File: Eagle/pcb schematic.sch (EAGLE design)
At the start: 19 parts

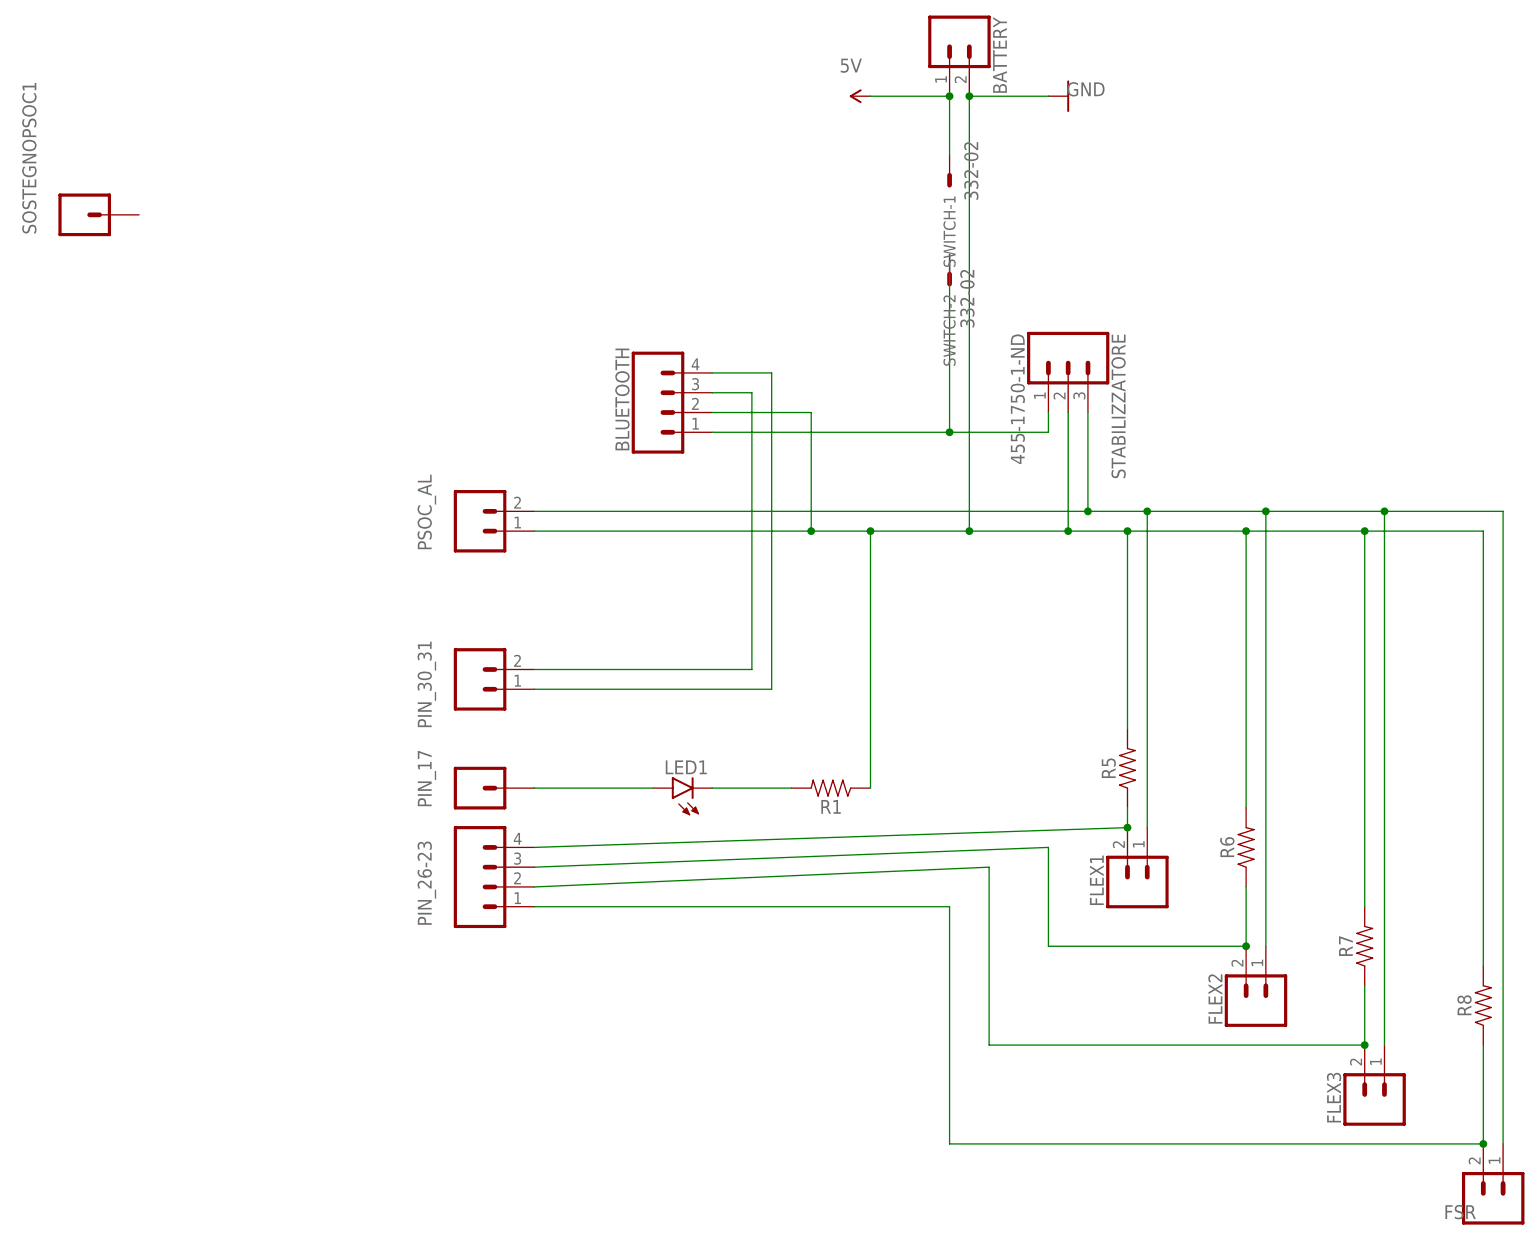
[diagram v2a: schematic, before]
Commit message: PCB con pin separati senza errori
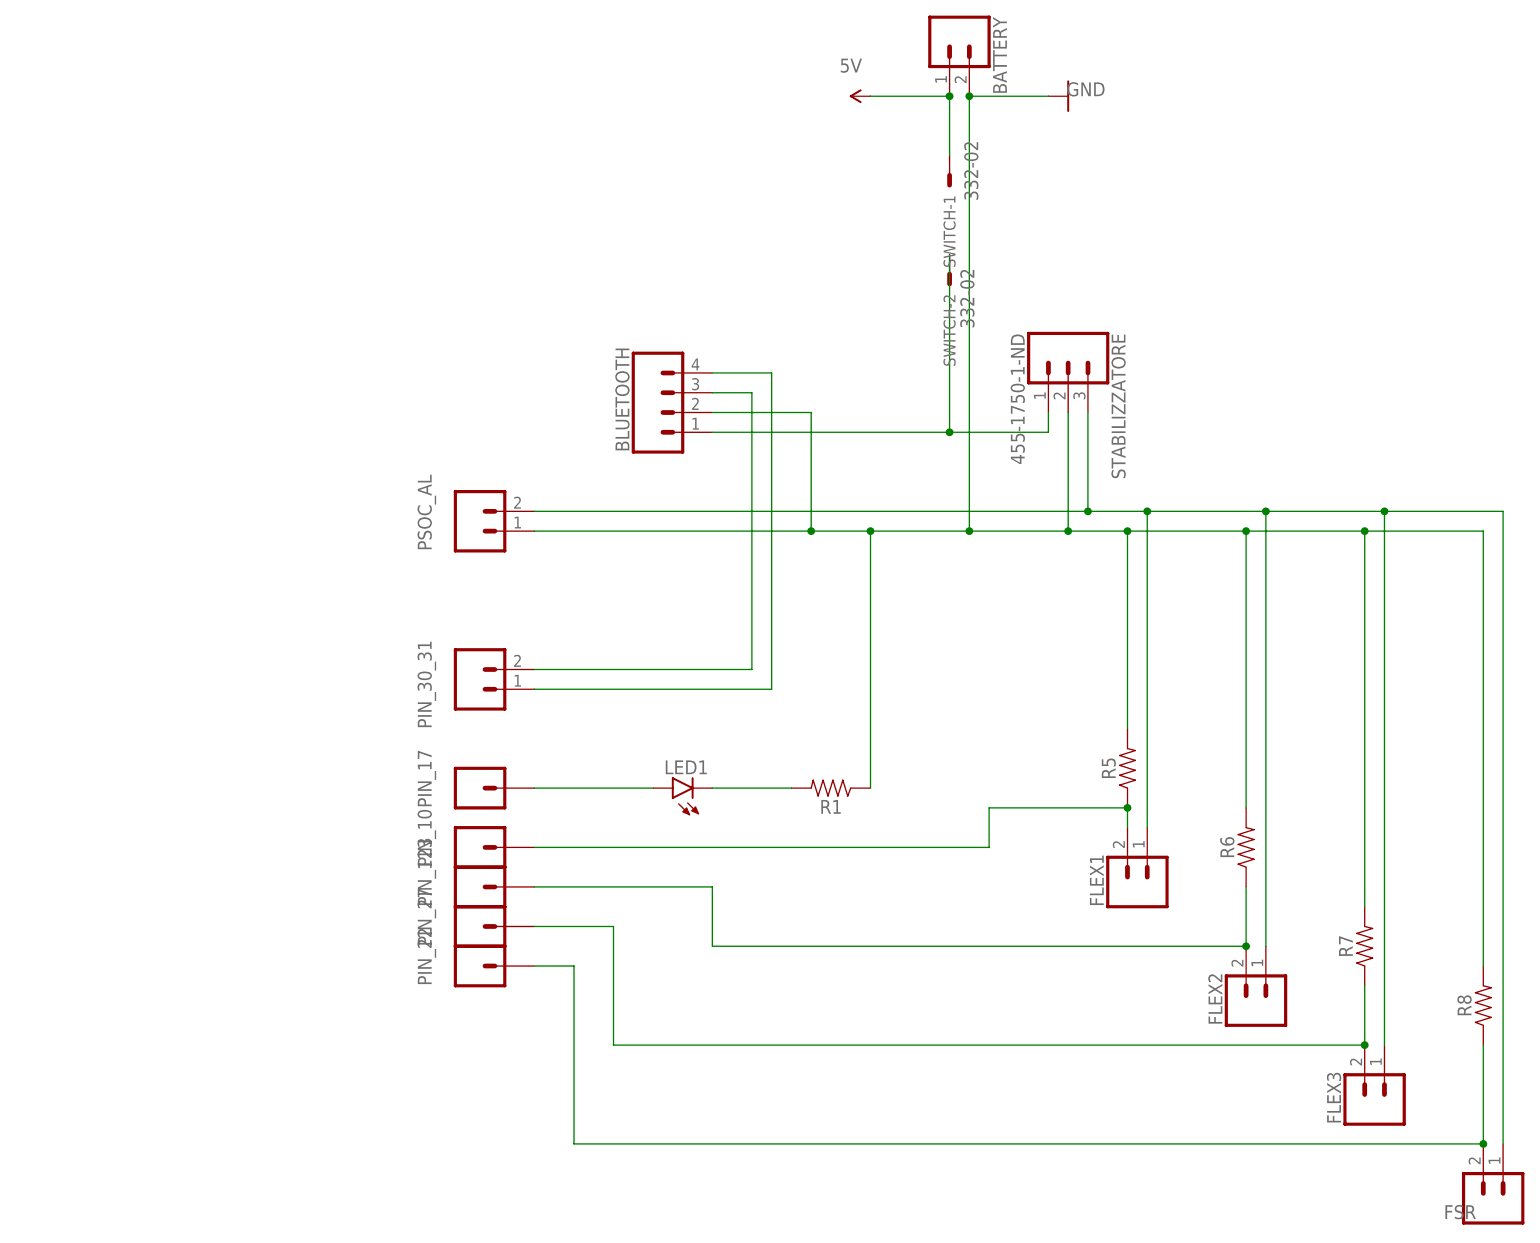
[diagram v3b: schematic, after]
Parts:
- removed PIN_26-23: (no value), SparkFun-Connectors:CONN_04
- removed SOSTEGNOPSOC1: (no value), SparkFun-Connectors:CONN_01
- added PIN_10, PIN_123, PIN_22, PIN_27: (no value), SparkFun-Connectors:CONN_01
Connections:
- net N$1: now also PIN_10.1; no longer PIN_26-23.4
- net N$2: now also PIN_123.1; no longer PIN_26-23.3
- net N$3: now also PIN_27.1; no longer PIN_26-23.2
- net N$5: now also PIN_22.1; no longer PIN_26-23.1
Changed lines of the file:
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@@
 <part name="FSR" library="SparkFun-Connectors" deviceset="CONN_02" device=""/>
 <part name="PSOC_AL" library="SparkFun-Connectors" deviceset="CONN_02" device=""/>
-<part name="PIN_26-23" library="SparkFun-Connectors" deviceset="CONN_04" device=""/>
 <part name="R5" library="SparkFun-Resistors" deviceset="RESISTOR" device="AXIAL-0.3" value=" "/>
 <part name="R6" library="SparkFun-Resistors" deviceset="RESISTOR" device="AXIAL-0.3" value=" "/>
@@
 <part name="LED1" library="led" library_urn="urn:adsk.eagle:library:259" deviceset="LED" device="5MM" package3d_urn="urn:adsk.eagle:package:15799/2"/>
 <part name="SWITCH" library="con-garry" library_urn="urn:adsk.eagle:library:147" deviceset="332-02" device="" package3d_urn="urn:adsk.eagle:package:6810/1"/>
-<part name="SOSTEGNOPSOC1" library="SparkFun-Connectors" deviceset="CONN_01" device=""/>
 <part name="STABILIZZATORE" library="SparkFun-Connectors" deviceset="CONN_03" device="" value="455-1750-1-ND"/>
+<part name="PIN_10" library="SparkFun-Connectors" deviceset="CONN_01" device=""/>
+<part name="PIN_123" library="SparkFun-Connectors" deviceset="CONN_01" device=""/>
+<part name="PIN_27" library="SparkFun-Connectors" deviceset="CONN_01" device=""/>
+<part name="PIN_22" library="SparkFun-Connectors" deviceset="CONN_01" device=""/>
 </parts>
 <sheets>
@@
 <attribute name="NAME" x="-61.468" y="71.12" size="1.778" layer="95" font="vector" rot="R90"/>
 </instance>
-<instance part="PIN_26-23" gate="G$1" x="-53.34" y="27.94" smashed="yes">
-<attribute name="VALUE" x="-58.42" y="20.574" size="1.778" layer="96" font="vector"/>
-<attribute name="NAME" x="-61.468" y="22.86" size="1.778" layer="95" font="vector" rot="R90"/>
-</instance>
 <instance part="R5" gate="G$1" x="27.94" y="43.18" smashed="yes" rot="R90">
 <attribute name="NAME" x="26.416" y="43.18" size="1.778" layer="95" font="vector" rot="R90" align="bottom-center"/>
@@
 <attribute name="VALUE" x="6.477" y="107.442" size="1.778" layer="96" rot="R270"/>
 </instance>
-<instance part="SOSTEGNOPSOC1" gate="G$1" x="-106.68" y="114.3" smashed="yes">
-<attribute name="VALUE" x="-109.22" y="109.474" size="1.778" layer="96" font="vector"/>
-<attribute name="NAME" x="-112.268" y="111.76" size="1.778" layer="95" font="vector" rot="R90"/>
-</instance>
 <instance part="STABILIZZATORE" gate="J$1" x="20.32" y="96.52" smashed="yes" rot="R270">
 <attribute name="VALUE" x="12.954" y="99.06" size="1.778" layer="96" font="vector" rot="R270"/>
 <attribute name="NAME" x="25.908" y="99.06" size="1.778" layer="95" font="vector" rot="R270"/>
+</instance>
+<instance part="PIN_10" gate="G$1" x="-55.88" y="33.02" smashed="yes">
+<attribute name="VALUE" x="-58.42" y="28.194" size="1.778" layer="96" font="vector"/>
+<attribute name="NAME" x="-61.468" y="30.48" size="1.778" layer="95" font="vector" rot="R90"/>
+</instance>
+<instance part="PIN_123" gate="G$1" x="-55.88" y="27.94" smashed="yes">
+<attribute name="VALUE" x="-58.42" y="23.114" size="1.778" layer="96" font="vector"/>
+<attribute name="NAME" x="-61.468" y="25.4" size="1.778" layer="95" font="vector" rot="R90"/>
+</instance>
+<instance part="PIN_27" gate="G$1" x="-55.88" y="22.86" smashed="yes">
+<attribute name="VALUE" x="-58.42" y="18.034" size="1.778" layer="96" font="vector"/>
+<attribute name="NAME" x="-61.468" y="20.32" size="1.778" layer="95" font="vector" rot="R90"/>
+</instance>
+<instance part="PIN_22" gate="G$1" x="-55.88" y="17.78" smashed="yes">
+<attribute name="VALUE" x="-58.42" y="12.954" size="1.778" layer="96" font="vector"/>
+<attribute name="NAME" x="-61.468" y="15.24" size="1.778" layer="95" font="vector" rot="R90"/>
 </instance>
 </instances>
@@
 <net name="N$2" class="0">
 <segment>
-<pinref part="PIN_26-23" gate="G$1" pin="3"/>
-<wire x1="-48.26" y1="30.48" x2="17.78" y2="33.02" width="0.1524" layer="91"/>
-<wire x1="17.78" y1="33.02" x2="17.78" y2="20.32" width="0.1524" layer="91"/>
 <pinref part="FLEX2" gate="G$1" pin="2"/>
-<wire x1="17.78" y1="20.32" x2="43.18" y2="20.32" width="0.1524" layer="91"/>
 <pinref part="R6" gate="G$1" pin="1"/>
 <wire x1="43.18" y1="20.32" x2="43.18" y2="27.94" width="0.1524" layer="91"/>
 <junction x="43.18" y="20.32"/>
+<wire x1="43.18" y1="20.32" x2="-25.4" y2="20.32" width="0.1524" layer="91"/>
+<wire x1="-25.4" y1="20.32" x2="-25.4" y2="27.94" width="0.1524" layer="91"/>
+<pinref part="PIN_123" gate="G$1" pin="1"/>
+<wire x1="-25.4" y1="27.94" x2="-48.26" y2="27.94" width="0.1524" layer="91"/>
 </segment>
 </net>
 <net name="N$3" class="0">
 <segment>
-<pinref part="PIN_26-23" gate="G$1" pin="2"/>
-<wire x1="-48.26" y1="27.94" x2="10.16" y2="30.48" width="0.1524" layer="91"/>
 <pinref part="FLEX3" gate="G$1" pin="2"/>
-<wire x1="10.16" y1="30.48" x2="10.16" y2="7.62" width="0.1524" layer="91"/>
-<wire x1="10.16" y1="7.62" x2="58.42" y2="7.62" width="0.1524" layer="91"/>
 <pinref part="R7" gate="G$1" pin="1"/>
 <wire x1="58.42" y1="15.24" x2="58.42" y2="7.62" width="0.1524" layer="91"/>
 <junction x="58.42" y="7.62"/>
+<wire x1="58.42" y1="7.62" x2="-38.1" y2="7.62" width="0.1524" layer="91"/>
+<wire x1="-38.1" y1="7.62" x2="-38.1" y2="22.86" width="0.1524" layer="91"/>
+<pinref part="PIN_27" gate="G$1" pin="1"/>
+<wire x1="-38.1" y1="22.86" x2="-48.26" y2="22.86" width="0.1524" layer="91"/>
 </segment>
 </net>
 <net name="N$1" class="0">
 <segment>
-<pinref part="PIN_26-23" gate="G$1" pin="4"/>
 <pinref part="FLEX1" gate="G$1" pin="2"/>
-<wire x1="-48.26" y1="33.02" x2="27.94" y2="35.56" width="0.1524" layer="91"/>
 <pinref part="R5" gate="G$1" pin="1"/>
-<junction x="27.94" y="35.56"/>
 <wire x1="27.94" y1="38.1" x2="27.94" y2="35.56" width="0.1524" layer="91"/>
+<pinref part="PIN_10" gate="G$1" pin="1"/>
+<wire x1="-48.26" y1="33.02" x2="10.16" y2="33.02" width="0.1524" layer="91"/>
+<wire x1="10.16" y1="33.02" x2="10.16" y2="38.1" width="0.1524" layer="91"/>
+<wire x1="10.16" y1="38.1" x2="27.94" y2="38.1" width="0.1524" layer="91"/>
+<junction x="27.94" y="38.1"/>
 </segment>
 </net>
@@
 <net name="N$5" class="0">
 <segment>
-<pinref part="PIN_26-23" gate="G$1" pin="1"/>
-<wire x1="-48.26" y1="25.4" x2="5.08" y2="25.4" width="0.1524" layer="91"/>
 <pinref part="FSR" gate="G$1" pin="2"/>
-<wire x1="73.66" y1="-5.08" x2="5.08" y2="-5.08" width="0.1524" layer="91"/>
-<wire x1="5.08" y1="-5.08" x2="5.08" y2="25.4" width="0.1524" layer="91"/>
+<wire x1="73.66" y1="-5.08" x2="-43.18" y2="-5.08" width="0.1524" layer="91"/>
 <pinref part="R8" gate="G$1" pin="1"/>
 <wire x1="73.66" y1="-5.08" x2="73.66" y2="7.62" width="0.1524" layer="91"/>
 <junction x="73.66" y="-5.08"/>
-</segment>
-</net>
+<wire x1="-43.18" y1="-5.08" x2="-43.18" y2="17.78" width="0.1524" layer="91"/>
+<pinref part="PIN_22" gate="G$1" pin="1"/>
+<wire x1="-43.18" y1="17.78" x2="-48.26" y2="17.78" width="0.1524" layer="91"/>
+</segment>
+</net>

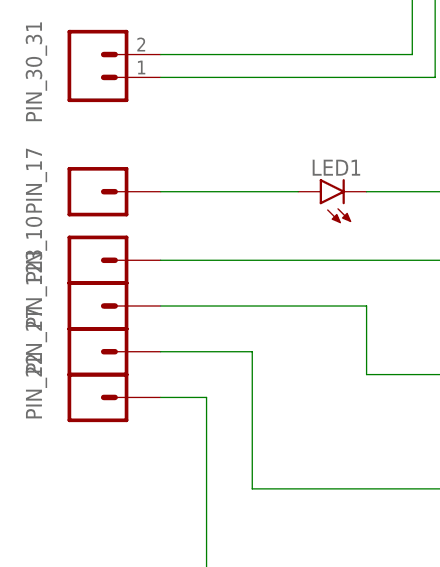
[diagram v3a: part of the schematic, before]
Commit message: PCB con pin separati senza errori
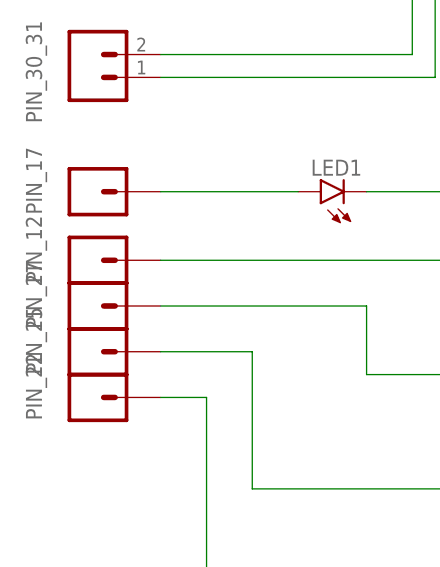
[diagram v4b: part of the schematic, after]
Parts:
- removed PIN_123: (no value), SparkFun-Connectors:CONN_01
- added PIN_25: (no value), SparkFun-Connectors:CONN_01
- renumbered PIN_10 to PIN_12
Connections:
- net N$2: now also PIN_27.1; no longer PIN_123.1
- net N$3: now also PIN_25.1; no longer PIN_27.1
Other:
- moved on the sheet: PIN_27
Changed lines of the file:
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@@
 <part name="SWITCH" library="con-garry" library_urn="urn:adsk.eagle:library:147" deviceset="332-02" device="" package3d_urn="urn:adsk.eagle:package:6810/1"/>
 <part name="STABILIZZATORE" library="SparkFun-Connectors" deviceset="CONN_03" device="" value="455-1750-1-ND"/>
-<part name="PIN_10" library="SparkFun-Connectors" deviceset="CONN_01" device=""/>
-<part name="PIN_123" library="SparkFun-Connectors" deviceset="CONN_01" device=""/>
+<part name="PIN_12" library="SparkFun-Connectors" deviceset="CONN_01" device=""/>
 <part name="PIN_27" library="SparkFun-Connectors" deviceset="CONN_01" device=""/>
+<part name="PIN_25" library="SparkFun-Connectors" deviceset="CONN_01" device=""/>
 <part name="PIN_22" library="SparkFun-Connectors" deviceset="CONN_01" device=""/>
 </parts>
@@
 <attribute name="NAME" x="25.908" y="99.06" size="1.778" layer="95" font="vector" rot="R270"/>
 </instance>
-<instance part="PIN_10" gate="G$1" x="-55.88" y="33.02" smashed="yes">
+<instance part="PIN_12" gate="G$1" x="-55.88" y="33.02" smashed="yes">
 <attribute name="VALUE" x="-58.42" y="28.194" size="1.778" layer="96" font="vector"/>
 <attribute name="NAME" x="-61.468" y="30.48" size="1.778" layer="95" font="vector" rot="R90"/>
 </instance>
-<instance part="PIN_123" gate="G$1" x="-55.88" y="27.94" smashed="yes">
+<instance part="PIN_27" gate="G$1" x="-55.88" y="27.94" smashed="yes">
 <attribute name="VALUE" x="-58.42" y="23.114" size="1.778" layer="96" font="vector"/>
 <attribute name="NAME" x="-61.468" y="25.4" size="1.778" layer="95" font="vector" rot="R90"/>
 </instance>
-<instance part="PIN_27" gate="G$1" x="-55.88" y="22.86" smashed="yes">
+<instance part="PIN_25" gate="G$1" x="-55.88" y="22.86" smashed="yes">
 <attribute name="VALUE" x="-58.42" y="18.034" size="1.778" layer="96" font="vector"/>
 <attribute name="NAME" x="-61.468" y="20.32" size="1.778" layer="95" font="vector" rot="R90"/>
@@
 <wire x1="43.18" y1="20.32" x2="-25.4" y2="20.32" width="0.1524" layer="91"/>
 <wire x1="-25.4" y1="20.32" x2="-25.4" y2="27.94" width="0.1524" layer="91"/>
-<pinref part="PIN_123" gate="G$1" pin="1"/>
+<pinref part="PIN_27" gate="G$1" pin="1"/>
 <wire x1="-25.4" y1="27.94" x2="-48.26" y2="27.94" width="0.1524" layer="91"/>
 </segment>
@@
 <wire x1="58.42" y1="7.62" x2="-38.1" y2="7.62" width="0.1524" layer="91"/>
 <wire x1="-38.1" y1="7.62" x2="-38.1" y2="22.86" width="0.1524" layer="91"/>
-<pinref part="PIN_27" gate="G$1" pin="1"/>
+<pinref part="PIN_25" gate="G$1" pin="1"/>
 <wire x1="-38.1" y1="22.86" x2="-48.26" y2="22.86" width="0.1524" layer="91"/>
 </segment>
@@
 <pinref part="R5" gate="G$1" pin="1"/>
 <wire x1="27.94" y1="38.1" x2="27.94" y2="35.56" width="0.1524" layer="91"/>
-<pinref part="PIN_10" gate="G$1" pin="1"/>
+<pinref part="PIN_12" gate="G$1" pin="1"/>
 <wire x1="-48.26" y1="33.02" x2="10.16" y2="33.02" width="0.1524" layer="91"/>
 <wire x1="10.16" y1="33.02" x2="10.16" y2="38.1" width="0.1524" layer="91"/>

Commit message: case finito + modifica pcb
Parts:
- renumbered PIN_30_31 to PIN_35_36
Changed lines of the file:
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@@
 <part name="PIN_17" library="SparkFun-Connectors" deviceset="CONN_01" device=""/>
 <part name="R1" library="SparkFun-Resistors" deviceset="RESISTOR" device="AXIAL-0.3" value=" "/>
-<part name="PIN_30_31" library="SparkFun-Connectors" deviceset="CONN_02" device=""/>
+<part name="PIN_35_36" library="SparkFun-Connectors" deviceset="CONN_02" device=""/>
 <part name="BATTERY" library="SparkFun-Connectors" deviceset="CONN_02" device=""/>
 <part name="BLUETOOTH" library="SparkFun-Connectors" deviceset="CONN_04" device=""/>
@@
 <attribute name="NAME" x="-10.16" y="39.116" size="1.778" layer="95" font="vector" rot="R180" align="bottom-center"/>
 </instance>
-<instance part="PIN_30_31" gate="G$1" x="-55.88" y="53.34" smashed="yes">
+<instance part="PIN_35_36" gate="G$1" x="-55.88" y="53.34" smashed="yes">
 <attribute name="VALUE" x="-58.42" y="48.514" size="1.778" layer="96" font="vector"/>
 <attribute name="NAME" x="-61.468" y="48.26" size="1.778" layer="95" font="vector" rot="R90"/>
@@
 <wire x1="-25.4" y1="91.44" x2="-20.32" y2="91.44" width="0.1524" layer="91"/>
 <wire x1="-20.32" y1="91.44" x2="-20.32" y2="55.88" width="0.1524" layer="91"/>
-<pinref part="PIN_30_31" gate="G$1" pin="2"/>
+<pinref part="PIN_35_36" gate="G$1" pin="2"/>
 <wire x1="-20.32" y1="55.88" x2="-48.26" y2="55.88" width="0.1524" layer="91"/>
 </segment>
@@
 <wire x1="-25.4" y1="93.98" x2="-17.78" y2="93.98" width="0.1524" layer="91"/>
 <wire x1="-17.78" y1="93.98" x2="-17.78" y2="53.34" width="0.1524" layer="91"/>
-<pinref part="PIN_30_31" gate="G$1" pin="1"/>
+<pinref part="PIN_35_36" gate="G$1" pin="1"/>
 <wire x1="-17.78" y1="53.34" x2="-48.26" y2="53.34" width="0.1524" layer="91"/>
 </segment>
